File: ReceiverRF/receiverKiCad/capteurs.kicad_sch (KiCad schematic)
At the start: 11 parts, among them J1 Conn_Coaxial, J3 Conn_01x04, U4 MLX90393SLW-ABA-011-RE

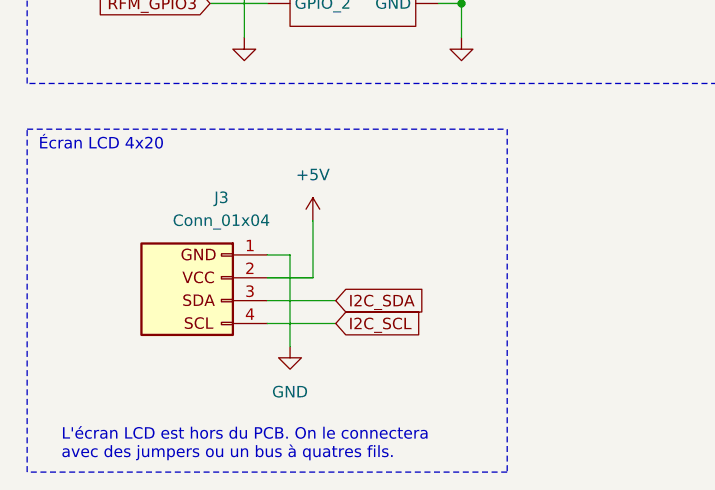
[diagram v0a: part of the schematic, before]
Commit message: suggestions de Luca et placement sur PCB
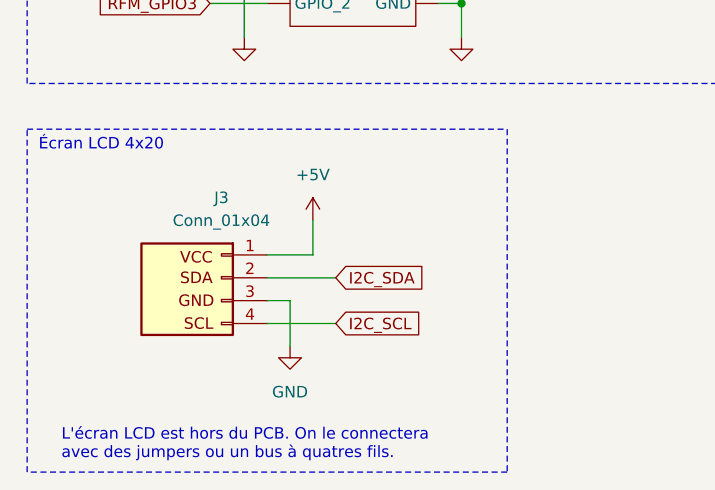
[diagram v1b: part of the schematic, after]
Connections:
- net +5V: now also J3.1 (GND); no longer J3.2 (VCC)
- net GND: now also J3.3 (SDA); no longer J3.1 (GND)
- net I2C_SDA: now also J3.2 (VCC); no longer J3.3 (SDA)
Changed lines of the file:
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@@
-	(wire
-		(pts
-			(xy 49.53 156.21) (xy 49.53 149.86)
-		)
-		(stroke
-			(width 0)
-			(type default)
-		)
-	)
 	(wire
 		(pts
@@
 	(wire
 		(pts
+			(xy 44.45 158.75) (xy 46.99 158.75)
+		)
+		(stroke
+			(width 0)
+			(type default)
+		)
+	)
+	(wire
+		(pts
 			(xy 92.71 62.23) (xy 92.71 73.66)
 		)
@@
 	(wire
 		(pts
-			(xy 44.45 156.21) (xy 49.53 156.21)
-		)
-		(stroke
-			(width 0)
-			(type default)
-		)
-	)
-	(wire
-		(pts
 			(xy 66.04 125.73) (xy 66.04 129.54)
 		)
@@
 	(wire
 		(pts
+			(xy 44.45 156.21) (xy 52.07 156.21)
+		)
+		(stroke
+			(width 0)
+			(type default)
+		)
+	)
+	(wire
+		(pts
+			(xy 44.45 153.67) (xy 49.53 153.67)
+		)
+		(stroke
+			(width 0)
+			(type default)
+		)
+	)
+	(wire
+		(pts
 			(xy 38.1 120.65) (xy 44.45 120.65)
 		)
@@
 	(wire
 		(pts
+			(xy 63.5 115.57) (xy 69.85 115.57)
+		)
+		(stroke
+			(width 0)
+			(type default)
+		)
+	)
+	(wire
+		(pts
+			(xy 40.64 69.85) (xy 40.64 54.61)
+		)
+		(stroke
+			(width 0)
+			(type default)
+		)
+	)
+	(wire
+		(pts
+			(xy 35.56 67.31) (xy 44.45 67.31)
+		)
+		(stroke
+			(width 0)
+			(type default)
+		)
+	)
+	(wire
+		(pts
+			(xy 63.5 107.95) (xy 66.04 107.95)
+		)
+		(stroke
+			(width 0)
+			(type default)
+		)
+	)
+	(wire
+		(pts
+			(xy 90.17 52.07) (xy 92.71 52.07)
+		)
+		(stroke
+			(width 0)
+			(type default)
+		)
+	)
+	(wire
+		(pts
+			(xy 46.99 158.75) (xy 46.99 163.83)
+		)
+		(stroke
+			(width 0)
+			(type default)
+		)
+	)
+	(wire
+		(pts
+			(xy 38.1 125.73) (xy 44.45 125.73)
+		)
+		(stroke
+			(width 0)
+			(type default)
+		)
+	)
+	(wire
+		(pts
+			(xy 110.49 62.23) (xy 110.49 64.77)
+		)
+		(stroke
+			(width 0)
+			(type default)
+		)
+	)
+	(wire
+		(pts
+			(xy 63.5 120.65) (xy 69.85 120.65)
+		)
+		(stroke
+			(width 0)
+			(type default)
+		)
+	)
+	(wire
+		(pts
+			(xy 63.5 125.73) (xy 66.04 125.73)
+		)
+		(stroke
+			(width 0)
+			(type default)
+		)
+	)
+	(wire
+		(pts
 			(xy 44.45 161.29) (xy 52.07 161.29)
 		)
@@
 	(wire
 		(pts
-			(xy 63.5 115.57) (xy 69.85 115.57)
-		)
-		(stroke
-			(width 0)
-			(type default)
-		)
-	)
-	(wire
-		(pts
-			(xy 40.64 69.85) (xy 40.64 54.61)
-		)
-		(stroke
-			(width 0)
-			(type default)
-		)
-	)
-	(wire
-		(pts
-			(xy 44.45 158.75) (xy 52.07 158.75)
-		)
-		(stroke
-			(width 0)
-			(type default)
-		)
-	)
-	(wire
-		(pts
-			(xy 35.56 67.31) (xy 44.45 67.31)
-		)
-		(stroke
-			(width 0)
-			(type default)
-		)
-	)
-	(wire
-		(pts
-			(xy 46.99 153.67) (xy 46.99 163.83)
-		)
-		(stroke
-			(width 0)
-			(type default)
-		)
-	)
-	(wire
-		(pts
-			(xy 63.5 107.95) (xy 66.04 107.95)
-		)
-		(stroke
-			(width 0)
-			(type default)
-		)
-	)
-	(wire
-		(pts
-			(xy 90.17 52.07) (xy 92.71 52.07)
-		)
-		(stroke
-			(width 0)
-			(type default)
-		)
-	)
-	(wire
-		(pts
-			(xy 38.1 125.73) (xy 44.45 125.73)
-		)
-		(stroke
-			(width 0)
-			(type default)
-		)
-	)
-	(wire
-		(pts
-			(xy 110.49 62.23) (xy 110.49 64.77)
-		)
-		(stroke
-			(width 0)
-			(type default)
-		)
-	)
-	(wire
-		(pts
-			(xy 63.5 120.65) (xy 69.85 120.65)
-		)
-		(stroke
-			(width 0)
-			(type default)
-		)
-	)
-	(wire
-		(pts
-			(xy 63.5 125.73) (xy 66.04 125.73)
-		)
-		(stroke
-			(width 0)
-			(type default)
-		)
-	)
-	(wire
-		(pts
-			(xy 44.45 153.67) (xy 46.99 153.67)
-		)
-		(stroke
-			(width 0)
-			(type default)
-		)
-	)
-	(wire
-		(pts
 			(xy 85.09 31.75) (xy 95.25 31.75)
 		)
@@
 		(pts
 			(xy 35.56 57.15) (xy 44.45 57.15)
+		)
+		(stroke
+			(width 0)
+			(type default)
+		)
+	)
+	(wire
+		(pts
+			(xy 49.53 153.67) (xy 49.53 149.86)
 		)
 		(stroke
@@
 	(global_label "I2C_SDA"
 		(shape input)
-		(at 52.07 158.75 0)
+		(at 52.07 156.21 0)
 		(fields_autoplaced yes)
 		(effects
@@
 		)
 		(property "Intersheetrefs" "${INTERSHEET_REFS}"
-			(at 62.6752 158.75 0)
-			(effects
-				(font
+			(at 62.6752 156.21 0)
+			(effects
+				(font

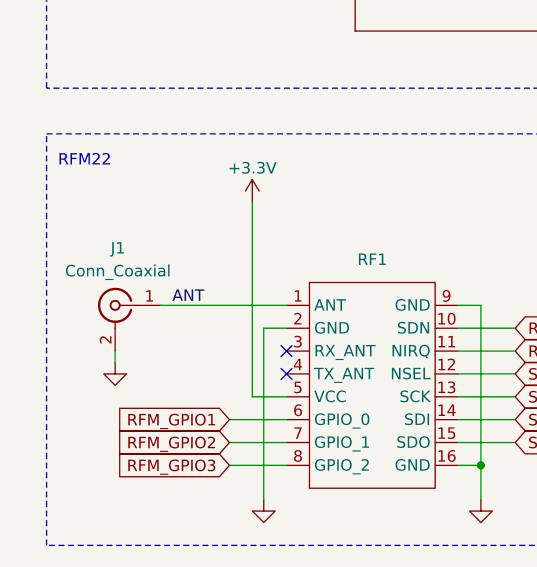
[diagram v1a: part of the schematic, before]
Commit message: impédance 50 ohm pour l'Antenne
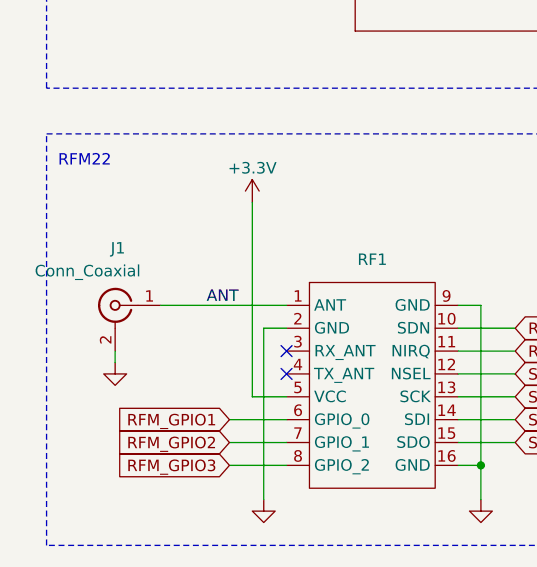
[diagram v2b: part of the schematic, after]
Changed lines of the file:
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@@
 	)
 	(label "ANT"
-		(at 31.75 107.95 0)
+		(at 35.56 107.95 0)
 		(fields_autoplaced yes)
 		(effects
@@
 		)
 	)
+	(netclass_flag ""
+		(length 2.54)
+		(shape round)
+		(at 31.75 107.95 0)
+		(effects
+			(font
+				(size 1.27 1.27)
+			)
+			(justify left bottom)
+		)
+		(property "Netclass" "50 ohm"
+			(at 29.972 103.886 0)
+			(effects
+				(font
+					(size 1.27 1.27)
+					(italic yes)
+				)
+				(justify left)
+			)
+		)
+	)
 	(symbol
 		(lib_id "power:GND")
@@
 		(on_board yes)
 		(dnp no)
-		(fields_autoplaced yes)
 		(property "Reference" "J1"
 			(at 25.7174 101.6 0)
@@
 		)
 		(property "Value" "Conn_Coaxial"
-			(at 25.7174 104.14 0)
-			(effects
-				(font
+			(at 22.352 104.14 0)
+			(effects
+				(font
